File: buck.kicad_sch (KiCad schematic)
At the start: 0 parts

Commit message: ldo and buck updated, footprints added
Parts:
- added C10, C14, C15, C17, C18, C19, C20, C21, C22: C_Polarized, symbol Device:C_Polarized
- added D3: D_Schottky, footprints4:SOD-523_0P9X1P3_ONS, symbol Device:D_Schottky
- added L1: SRN1060-101M, footprints7:IND_BOURNS_SRN1060, symbol Device:L
- added Q4, Q5: AO3400A, Package_TO_SOT_SMD:SOT-23, symbol Simulation_SPICE:NMOS
- added R26, R27, R28, R29, R30, R31, R32, R33: R, symbol Device:R
- added TP10, TP11, TP12, TP13, TP14, TP15, TP16, TP17, TP18, TP9: TestPoint, TestPoint:TestPoint_Pad_D1.0mm, symbol Connector:TestPoint
- added U10: TLV9101IDBVR, footprints6:DBV0005A_TEX, symbol Simulation_SPICE:OPAMP
- added U13: ${SIM.PARAMS}, symbol Simulation_SPICE:OPAMP
- added U14: SL78L05, Package_TO_SOT_SMD:SOT-89-3, symbol Regulator_Linear:LT1963AxST-3.3
- added U17: MIC4605-2YM-TR, footprints5:SOIC-8_M_MCH, symbol 2026-04-21_21-30-44:MIC4605-2YM-TR
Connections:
- new net: C10.2, D3.1 (K), R26.1, U17.4 (HS)
- new net: C10.1, TP17.1, U17.2 (HB)
- new net: C21.2, R27.2, R28.1, R29.2, R30.2, R31.2, R32.2, R33.2, TP15.1, U10.4 (-)
- new net: C22.2, R30.1
- new net: C20.2, R29.1
- new net +3.5V: C14.1, C15.1, C17.1, C18.1, C19.1, C20.1, L1.2, R27.1, R31.1, R32.1, R33.1, TP10.1
- new net +5V: TP18.1, U13.3 (V+), U14.1 (OUT)
- new net +9V: Q4.3 (D), U10.5 (V+), U14.3 (IN), U17.1 (VDD)
- new net GND: C14.2, C15.2, C17.2, C18.2, C19.2, D3.2 (A), Q5.3 (D), R28.2, U10.2 (V-), U13.4 (V-), U14.2 (GND), U17.7 (VSS)
- new net Sawtooth Generator/sawtooth: TP14.1, U13.2 (-)
- new net error: C21.1, C22.1, TP16.1, U10.1, U13.1 (+)
- new net high: Q4.1 (G), TP11.1, U17.3 (HO)
- new net low: Q5.1 (G), TP12.1, U17.8 (LO)
- new net pwm: TP13.1, U13.5, U17.5 (PWM)
- new net switch_node: L1.1, Q4.2 (S), Q5.2 (S), R26.2, TP9.1
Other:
- added sheet Sawtooth Generator (sawtoothgenerator.kicad_sch)

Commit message: schematic cleanup
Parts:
- added U21: MCP6571T-E/OT, footprints:SOP_MCP6571T-E&slash_OT_MCH, symbol Simulation_SPICE:OPAMP
- C10, C14, C15, C17, C18, C19, C20, C21, C22: footprint (none) -> Capacitor_SMD:C_0805_2012Metric; symbol Device:C_Polarized -> Device:C
- D3: footprint footprints4:SOD-523_0P9X1P3_ONS -> Diode_SMD:D_SOD-523
- L1: footprint footprints7:IND_BOURNS_SRN1060 -> footprints:IND_BOURNS_SRN1060
- R26, R27, R28, R29, R30, R31, R32, R33: footprint (none) -> Resistor_SMD:R_0805_2012Metric
- U13: value ${SIM.PARAMS} -> MCP6571T-E/OT; footprint (none) -> footprints:SOP_MCP6571T-E&slash_OT_MCH
- U17: footprint footprints5:SOIC-8_M_MCH -> footprints:SOIC-8_M_MCH
- U20: renamed from U10; footprint footprints6:DBV0005A_TEX -> footprints:DBV0005A_TEX
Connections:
- net +5V: now also U21.5 (V+); no longer U13.3 (V+)
- net GND: now also U21.2 (V-); no longer U13.4 (V-)
- net Sawtooth Generator/sawtooth: now also U21.4 (-); no longer U13.2 (-)
- net error: now also U21.3 (+); no longer U13.1 (+)
- net pwm: now also U21.1; no longer U13.5
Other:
- sheet Sawtooth Generator ports: added I_PTAT; removed none
- moved on the sheet: TP13

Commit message: adc PCB
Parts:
- removed U13: MCP6571T-E/OT, footprints:SOP_MCP6571T-E&slash_OT_MCH, symbol Simulation_SPICE:OPAMP
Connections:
- net +5V: now also U21.6 (V+); no longer U21.5 (V+)
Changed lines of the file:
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@@
 	)
 	(symbol
-		(lib_name "OPAMP_1")
+		(lib_name "OPAMP_2")
 		(lib_id "Simulation_SPICE:OPAMP")
 		(at 77.47 118.11 180)
@@
 		(pin "1"
 		)
-		(pin "5"
+		(pin "6"
 		)
 		(pin "3"
@@
 					(unit 1)
 				)
-			)
-		)
-	)
-	(symbol
-		(lib_name "OPAMP_1")
-		(lib_id "Simulation_SPICE:OPAMP")
-		(at 74.93 138.43 0)
-		(mirror x)
-		(unit 1)
-		(exclude_from_sim no)
-		(in_bom yes)
-		(on_board yes)
-		(dnp no)
-		(property "Reference" "U13"
-			(at 83.82 143.5802 0)
-			(effects
-				(font
-					(size 1.27 1.27)
-				)
-			)
-		)
-		(property "Value" "MCP6571T-E/OT"
-			(at 83.82 141.6751 0)
-			(effects
-				(font
-					(size 1.27 1.27)
-				)
-			)
-		)
-		(property "Footprint" "footprints:SOP_MCP6571T-E&slash_OT_MCH"
-			(at 74.93 138.43 0)
-			(effects
-				(font
-					(size 1.27 1.27)
-				)
-				(hide yes)
-			)
-		)
-		(property "Datasheet" "https://ngspice.sourceforge.io/docs/ngspice-html-manual/manual.xhtml#sec__SUBCKT_Subcircuits"
-			(at 74.93 138.43 0)
-			(effects
-				(font
-					(size 1.27 1.27)
-				)
-				(hide yes)
-			)
-		)
-		(property "Description" "Operational amplifier, single"
-			(at 74.93 138.43 0)
-			(effects
-				(font
-					(size 1.27 1.27)
-				)
-				(hide yes)
-			)
-		)
-		(property "Sim.Pins" "1=in+ 2=in- 3=vcc 4=vee 5=out"
-			(at 74.93 138.43 0)
-			(effects
-				(font
-					(size 1.27 1.27)
-				)
-				(hide yes)
-			)
-		)
-		(property "Sim.Device" "SUBCKT"
-			(at 74.93 138.43 0)
-			(effects
-				(font
-					(size 1.27 1.27)
-				)
-				(justify left)
-				(hide yes)
-			)
-		)
-		(property "Sim.Library" "${KICAD9_SYMBOL_DIR}/Simulation_SPICE.sp"
-			(at 74.93 138.43 0)
-			(effects
-				(font
-					(size 1.27 1.27)
-				)
-				(hide yes)
-			)
-		)
-		(property "Sim.Name" "kicad_builtin_opamp"
-			(at 74.93 138.43 0)
-			(effects
-				(font
-					(size 1.27 1.27)
-				)
-				(hide yes)
-			)
-		)
-		(pin "2"
-		)
-		(pin "1"
-		)
-		(pin "5"
-		)
-		(pin "3"
-		)
-		(pin "4"
-		)
-		(instances
-			(project "ee115-capstone"
-				(path "/80dfed98-7d85-4c9a-bb85-182165e7352f/7b7808b9-ad0e-40e5-acbd-cc767749d54b"
-					(reference "U13")
-					(unit 1)
-				)

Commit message: pcb layout
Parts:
- added C26, C27, C28, C29, C30, C31, C32, C33, C34, C35, C36, C37, C38, C39, C40, C48, C49: C_Polarized, Capacitor_SMD:C_0805_2012Metric, symbol Device:C
- added R30, R46, R47, R48, R50, R51, R52, R53, R54, Re1, Re2, Re3, Re4: R, Resistor_SMD:R_0805_2012Metric, symbol Device:R
- TP10, TP11, TP12, TP13, TP14, TP15, TP16, TP17, TP18, TP9: footprint TestPoint:TestPoint_Pad_D1.0mm -> TestPoint:TestPoint_Plated_Hole_D2.0mm
- U20: value TLV9101IDBVR -> AD8038; footprint footprints:DBV0005A_TEX -> footprints_pretty:KS_5_ADI
- renumbered R30 to R67
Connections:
- net +3.5V: now also C26.1, C27.1, C28.1, C29.1, R30.1
- net +5V: now also C40.1, C48.2
- net +9V: now also C38.1, C39.1, C49.1
- net GND: now also C38.2, C39.2, C40.2, C48.1, C49.2, R51.2, R52.2, R53.2, R54.2
- net error: now also C30.1, C31.1, C32.1, C33.1, C34.1, C35.1, C36.1, C37.1
- net at C21.2, R27.2, R28.1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: now also C30.2, C31.2, C32.2, C33.2, R30.2, R46.2, R47.2, R48.2, R50.2, R51.1, R52.1, R53.1, R54.1, Re1.2, Re2.2, Re3.2, Re4.2
- net at C22.2, R67.1: now also C34.2, C35.2, C36.2, C37.2, Re1.1, Re2.1, Re3.1, Re4.1
- net at C20.2, R29.1: now also C26.2, C27.2, C28.2, C29.2, R46.1, R47.1, R48.1, R50.1
- net bg_volt: now reaches U20.3 (+)
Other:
- moved on the sheet: C20, C21, R27, R28, R29, R31, R32, R33, R67

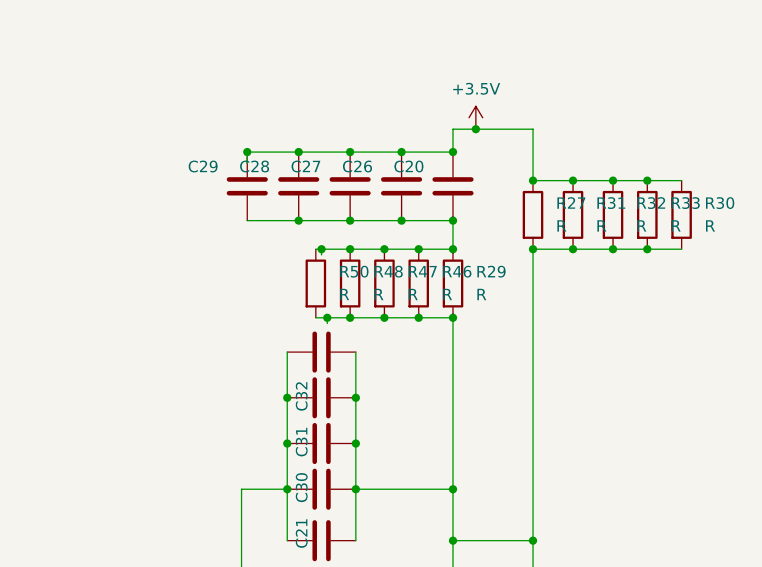
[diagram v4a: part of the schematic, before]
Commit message: pcb layout component placement 90% done
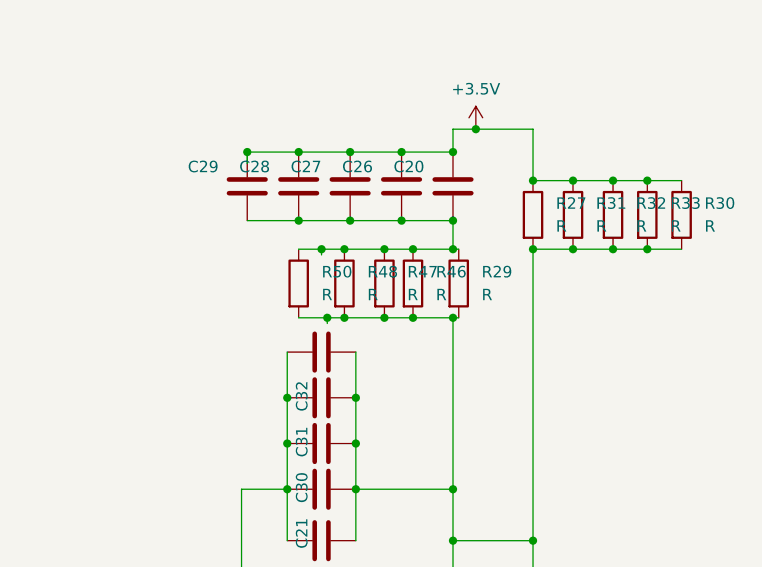
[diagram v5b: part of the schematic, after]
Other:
- moved on the sheet: R29, R46, R48, R50
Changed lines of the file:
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@@
 	)
 	(junction
+		(at 238.76 76.835)
+		(diameter 0)
+		(color 0 0 0 0)
+	)
+	(junction
 		(at 227.965 58.42)
 		(diameter 0)
@@
 	)
 	(junction
+		(at 238.76 69.215)
+		(diameter 0)
+		(color 0 0 0 0)
+	)
+	(junction
 		(at 250.825 69.215)
 		(diameter 0)
@@
 	)
 	(junction
-		(at 247.015 76.835)
-		(diameter 0)
-		(color 0 0 0 0)
-	)
-	(junction
 		(at 239.395 58.42)
 		(diameter 0)
@@
 	)
 	(junction
+		(at 246.38 69.215)
+		(diameter 0)
+		(color 0 0 0 0)
+	)
+	(junction
 		(at 250.825 76.835)
 		(diameter 0)
@@
 	)
 	(junction
-		(at 247.015 69.215)
+		(at 264.16 69.215)
 		(diameter 0)
 		(color 0 0 0 0)
 	)
 	(junction
-		(at 264.16 69.215)
+		(at 250.825 66.04)
 		(diameter 0)
 		(color 0 0 0 0)
 	)
 	(junction
-		(at 250.825 66.04)
+		(at 272.415 61.595)
 		(diameter 0)
 		(color 0 0 0 0)
 	)
 	(junction
-		(at 272.415 61.595)
+		(at 246.38 76.835)
 		(diameter 0)
 		(color 0 0 0 0)
@@
 	)
 	(junction
-		(at 239.395 76.835)
-		(diameter 0)
-		(color 0 0 0 0)
-	)
-	(junction
 		(at 262.89 138.43)
 		(diameter 0)
@@
 	)
 	(junction
-		(at 239.395 69.215)
-		(diameter 0)
-		(color 0 0 0 0)
-	)
-	(junction
 		(at 262.89 146.05)
 		(diameter 0)
@@
 	(wire
 		(pts
-			(xy 247.015 69.215) (xy 250.825 69.215)
-		)
-		(stroke
-			(width 0)
-			(type default)
-		)
-	)
-	(wire
-		(pts
 			(xy 113.665 85.725) (xy 113.665 88.9)
 		)
@@
 	(wire
 		(pts
-			(xy 243.205 76.835) (xy 247.015 76.835)
+			(xy 243.205 76.835) (xy 246.38 76.835)
 		)
 		(stroke
@@
 	(wire
 		(pts
+			(xy 246.38 69.215) (xy 250.825 69.215)
+		)
+		(stroke
+			(width 0)
+			(type default)
+		)
+	)
+	(wire
+		(pts
 			(xy 153.67 73.025) (xy 153.67 73.66)
 		)
@@
 	(wire
 		(pts
-			(xy 235.585 69.215) (xy 236.22 69.215)
+			(xy 233.68 69.215) (xy 236.22 69.215)
 		)
 		(stroke
@@
 	(wire
 		(pts
-			(xy 239.395 69.215) (xy 243.205 69.215)
+			(xy 31.75 104.14) (xy 31.75 107.315)
 		)
 		(stroke
@@
 	(wire
 		(pts
-			(xy 31.75 104.14) (xy 31.75 107.315)
+			(xy 153.67 80.645) (xy 159.385 80.645)
 		)
 		(stroke
@@
 	(wire
 		(pts
-			(xy 153.67 80.645) (xy 159.385 80.645)
+			(xy 248.285 154.305) (xy 248.285 143.51)
 		)
 		(stroke
@@
 	(wire
 		(pts
-			(xy 248.285 154.305) (xy 248.285 143.51)
+			(xy 238.76 69.215) (xy 243.205 69.215)
 		)
 		(stroke
@@
 	(wire
 		(pts
-			(xy 121.92 93.98) (xy 121.92 94.615)
+			(xy 251.46 76.835) (xy 250.825 76.835)
 		)
 		(stroke
@@
 	(wire
 		(pts
-			(xy 245.11 128.27) (xy 245.11 127.635)
+			(xy 121.92 93.98) (xy 121.92 94.615)
 		)
 		(stroke
@@
 	(wire
 		(pts
-			(xy 239.395 76.835) (xy 243.205 76.835)
+			(xy 245.11 128.27) (xy 245.11 127.635)
 		)
 		(stroke
@@
 	(wire
 		(pts
+			(xy 238.76 76.835) (xy 243.205 76.835)
+		)
+		(stroke
+			(width 0)
+			(type default)
+		)
+	)
+	(wire
+		(pts
 			(xy 227.965 58.42) (xy 233.68 58.42)
 		)
@@
 	(wire
 		(pts
-			(xy 243.205 69.215) (xy 247.015 69.215)
+			(xy 243.205 69.215) (xy 246.38 69.215)
 		)
 		(stroke
@@
 	(wire
 		(pts
-			(xy 247.015 76.835) (xy 250.825 76.835)
-		)
-		(stroke
-			(width 0)
-			(type default)
-		)
-	)
-	(wire
-		(pts
 			(xy 95.25 90.17) (xy 96.52 90.17)
 		)
@@
 	(wire
 		(pts
-			(xy 236.22 69.215) (xy 239.395 69.215)
+			(xy 236.22 69.215) (xy 238.76 69.215)
 		)
 		(stroke
@@
 	(wire
 		(pts
-			(xy 235.585 76.835) (xy 236.855 76.835)
+			(xy 233.68 76.835) (xy 236.855 76.835)
 		)
 		(stroke
@@
 	(wire
 		(pts
-			(xy 236.855 76.835) (xy 239.395 76.835)
+			(xy 236.855 76.835) (xy 238.76 76.835)
 		)
 		(stroke
@@
 	(wire
 		(pts
+			(xy 251.46 69.215) (xy 250.825 69.215)
+		)
+		(stroke
+			(width 0)
+			(type default)
+		)
+	)
+	(wire
+		(pts
 			(xy 73.025 46.99) (xy 73.025 62.865)
 		)
@@
 	(wire
 		(pts
+			(xy 246.38 76.835) (xy 250.825 76.835)
+		)
+		(stroke
+			(width 0)
+			(type default)
+		)
+	)
+	(wire
+		(pts
 			(xy 34.925 102.235) (xy 34.925 102.87)
 		)
@@
 	(symbol
 		(lib_id "Device:R")
-		(at 247.015 73.025 0)
+		(at 246.38 73.025 0)
 		(unit 1)
 		(exclude_from_sim no)
@@
 		(fields_autoplaced yes)
 		(property "Reference" "R46"
-			(at 249.555 71.7549 0)
+			(at 248.92 71.7549 0)
 			(effects
 				(font
@@
 		)
 		(property "Value" "R"
-			(at 249.555 74.2949 0)
+			(at 248.92 74.2949 0)
 			(effects
 				(font
@@
 		)
 		(property "Footprint" "Resistor_SMD:R_0805_2012Metric"
-			(at 245.237 73.025 90)
+			(at 244.602 73.025 90)
 			(effects
 				(font
@@
 		)
 		(property "Datasheet" "~"
-			(at 247.015 73.025 0)
+			(at 246.38 73.025 0)
 			(effects
 				(font
@@
 		)
 		(property "Description" "Resistor"
-			(at 247.015 73.025 0)
+			(at 246.38 73.025 0)
 			(effects
 				(font
@@
 	(symbol
 		(lib_id "Device:R")
-		(at 235.585 73.025 0)
+		(at 233.68 73.025 0)
 		(unit 1)
 		(exclude_from_sim no)
@@
 		(fields_autoplaced yes)
 		(property "Reference" "R50"
-			(at 238.125 71.7549 0)
+			(at 236.22 71.7549 0)
 			(effects
 				(font
@@
 		)
 		(property "Value" "R"
-			(at 238.125 74.2949 0)
+			(at 236.22 74.2949 0)
 			(effects
 				(font
@@
 		)
 		(property "Footprint" "Resistor_SMD:R_0805_2012Metric"
-			(at 233.807 73.025 90)
+			(at 231.902 73.025 90)
 			(effects
 				(font
@@
 		)
 		(property "Datasheet" "~"
-			(at 235.585 73.025 0)
+			(at 233.68 73.025 0)
 			(effects
 				(font
@@
 		)
 		(property "Description" "Resistor"
-			(at 235.585 73.025 0)
+			(at 233.68 73.025 0)
 			(effects
 				(font
@@
 	(symbol
 		(lib_id "Device:R")
-		(at 250.825 73.025 0)
+		(at 251.46 73.025 0)
 		(unit 1)
 		(exclude_from_sim no)
@@
 		(fields_autoplaced yes)
 		(property "Reference" "R29"
-			(at 253.365 71.7549 0)
+			(at 254 71.7549 0)
 			(effects
 				(font
@@
 		)
 		(property "Value" "R"
-			(at 253.365 74.2949 0)
+			(at 254 74.2949 0)
 			(effects
 				(font
@@
 		)
 		(property "Footprint" "Resistor_SMD:R_0805_2012Metric"
-			(at 249.047 73.025 90)
+			(at 249.682 73.025 90)
 			(effects
 				(font
@@
 		)
 		(property "Datasheet" "~"
-			(at 250.825 73.025 0)
+			(at 251.46 73.025 0)
 			(effects
 				(font
@@
 		)
 		(property "Description" "Resistor"
-			(at 250.825 73.025 0)
+			(at 251.46 73.025 0)
 			(effects
 				(font
@@
 	(symbol
 		(lib_id "Device:R")
-		(at 239.395 73.025 0)
+		(at 238.76 73.025 0)
 		(unit 1)
 		(exclude_from_sim no)
@@
 		(fields_autoplaced yes)
 		(property "Reference" "R48"
-			(at 241.935 71.7549 0)
+			(at 241.3 71.7549 0)
 			(effects
 				(font
@@
 		)
 		(property "Value" "R"
-			(at 241.935 74.2949 0)
+			(at 241.3 74.2949 0)
 			(effects
 				(font
@@
 		)
 		(property "Footprint" "Resistor_SMD:R_0805_2012Metric"
-			(at 237.617 73.025 90)
+			(at 236.982 73.025 90)
 			(effects
 				(font
@@
 		)
 		(property "Datasheet" "~"
-			(at 239.395 73.025 0)
+			(at 238.76 73.025 0)
 			(effects
 				(font
@@
 		)
 		(property "Description" "Resistor"
-			(at 239.395 73.025 0)
+			(at 238.76 73.025 0)
 			(effects
 				(font
